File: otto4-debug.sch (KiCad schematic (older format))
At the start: 1 part

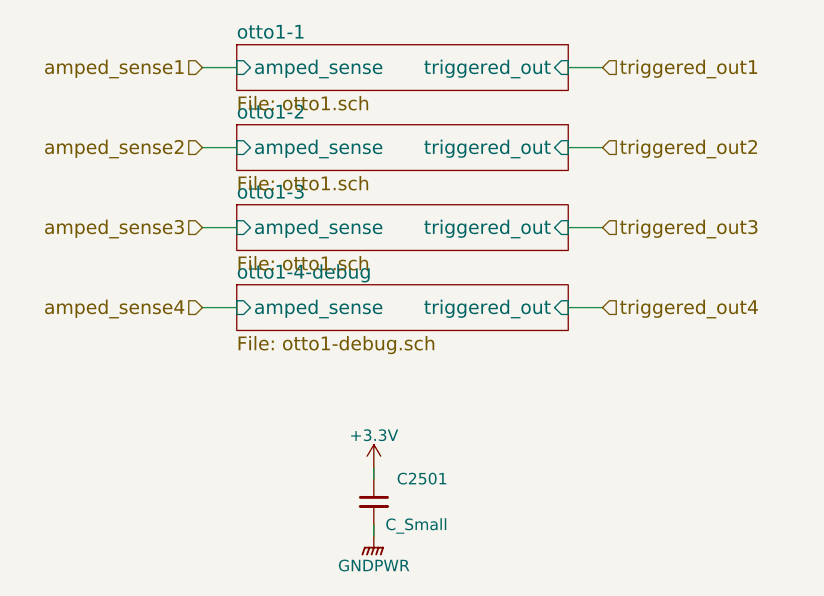
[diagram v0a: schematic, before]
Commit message: fixed debug pin going to multiple units
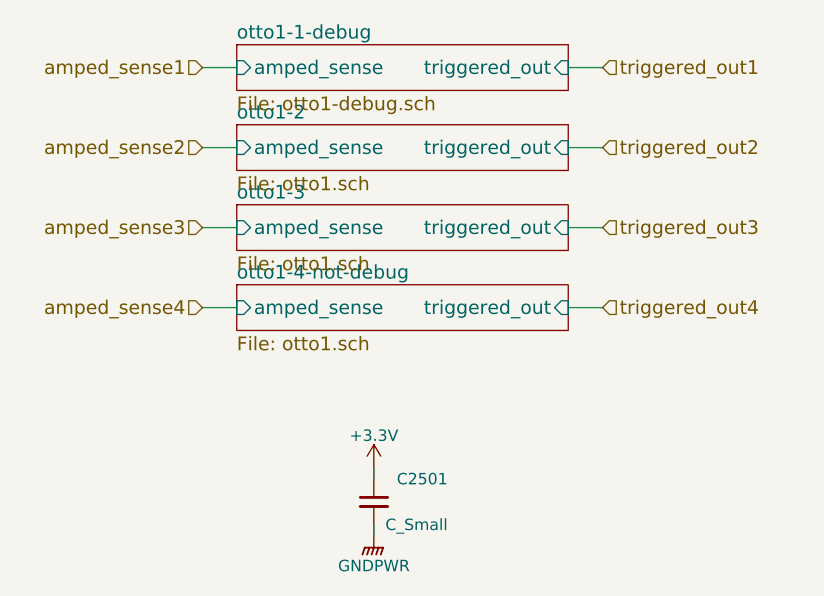
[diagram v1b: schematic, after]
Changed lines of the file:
@@
 $Sheet
 S 1550 1750 1450 200
-U 5AFCC6B4
-F0 "otto1-1" 60
-F1 "otto1.sch" 60
+U 5B02385F
+F0 "otto1-1-debug" 60
+F1 "otto1-debug.sch" 60
 F2 "amped_sense" I L 1550 1850 60
 F3 "triggered_out" I R 3000 1850 60
@@
 S 1550 2800 1450 200
 U 5AFCD579
-F0 "otto1-4-debug" 60
-F1 "otto1-debug.sch" 60
+F0 "otto1-4-not-debug" 60
+F1 "otto1.sch" 60
 F2 "amped_sense" I L 1550 2900 60
 F3 "triggered_out" I R 3000 2900 60
@@
 $Comp
 L C_Small C2501
-U 1 1 5B007FCB
+U 1 1 5B02386C
 P 2150 3750
-AR Path="/5AFCE970/5AFFB716/5AFCC2D5/5B007FCB" Ref="C2501"  Part="1"
-AR Path="/5AFCE970/5AFFB716/5AFCF0A3/5B007FCB" Ref="C3001"  Part="1"
-AR Path="/5AFCE970/5AFFB716/5AFD08C6/5B007FCB" Ref="C3501"  Part="1"
 F 0 "C2501" H 2250 3850 50  0000 L CNN
 F 1 "C_Small" H 2200 3650 50  0000 L CNN
@@
 $Comp
 L +3.3V #PWR?
-U 1 1 5B007FD7
+U 1 1 5B02386D
 P 2150 3600
-AR Path="/5AFCE970/5AFFB716/5AFCC2D5/5B007FD7" Ref="#PWR?"  Part="1"
-AR Path="/5AFCE970/5AFFB716/5AFCF0A3/5B007FD7" Ref="#PWR?"  Part="1"
-AR Path="/5AFCE970/5AFFB716/5AFD08C6/5B007FD7" Ref="#PWR?"  Part="1"
 F 0 "#PWR?" H 2150 3450 50  0001 C CNN
 F 1 "+3.3V" H 2150 3740 50  0000 C CNN
@@
 $Comp
 L GNDPWR #PWR?
-U 1 1 5B0088D8
+U 1 1 5B02386E
 P 2150 3900
-AR Path="/5AFCE970/5AFFB716/5AFCC2D5/5B0088D8" Ref="#PWR?"  Part="1"
-AR Path="/5AFCE970/5AFFB716/5AFCF0A3/5B0088D8" Ref="#PWR?"  Part="1"
-AR Path="/5AFCE970/5AFFB716/5AFD08C6/5B0088D8" Ref="#PWR?"  Part="1"
 F 0 "#PWR?" H 2150 3700 50  0001 C CNN
 F 1 "GNDPWR" H 2150 3770 50  0000 C CNN

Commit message: debugging is on lowest channel now
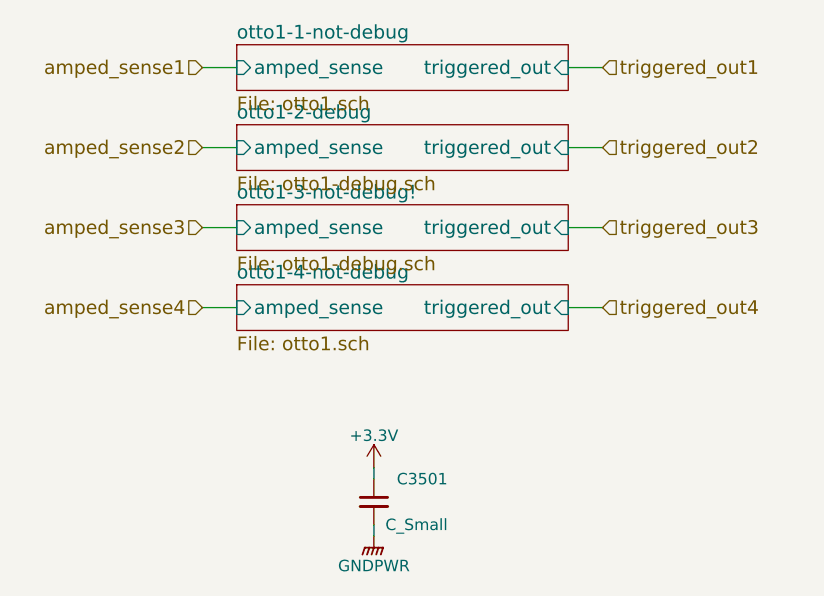
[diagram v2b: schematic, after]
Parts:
- renumbered C2501 to C3501
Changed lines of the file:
@@
 $Descr A4 11693 8268
 encoding utf-8
-Sheet 25 41
+Sheet 35 41
 Title ""
 Date ""
@@
 S 1550 1750 1450 200
 U 5B02385F
-F0 "otto1-1-debug" 60
-F1 "otto1-debug.sch" 60
+F0 "otto1-1-not-debug" 60
+F1 "otto1.sch" 60
 F2 "amped_sense" I L 1550 1850 60
 F3 "triggered_out" I R 3000 1850 60
@@
 S 1550 2100 1450 200
 U 5AFCD431
-F0 "otto1-2" 60
-F1 "otto1.sch" 60
+F0 "otto1-2-debug" 60
+F1 "otto1-debug.sch" 60
 F2 "amped_sense" I L 1550 2200 60
 F3 "triggered_out" I R 3000 2200 60
@@
 S 1550 2450 1450 200
 U 5AFCD50F
-F0 "otto1-3" 60
-F1 "otto1.sch" 60
+F0 "otto1-3-not-debug!" 60
+F1 "otto1-debug.sch" 60
 F2 "amped_sense" I L 1550 2550 60
 F3 "triggered_out" I R 3000 2550 60
@@
 	3000 2900 3150 2900
 $Comp
-L C_Small C2501
+L C_Small C3501
 U 1 1 5B02386C
 P 2150 3750
-F 0 "C2501" H 2250 3850 50  0000 L CNN
+F 0 "C3501" H 2250 3850 50  0000 L CNN
 F 1 "C_Small" H 2200 3650 50  0000 L CNN
 F 2 "Resistors_SMD:R_0805_HandSoldering" H 2150 3750 50  0001 C CNN

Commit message: started on routing triggers to blue pill
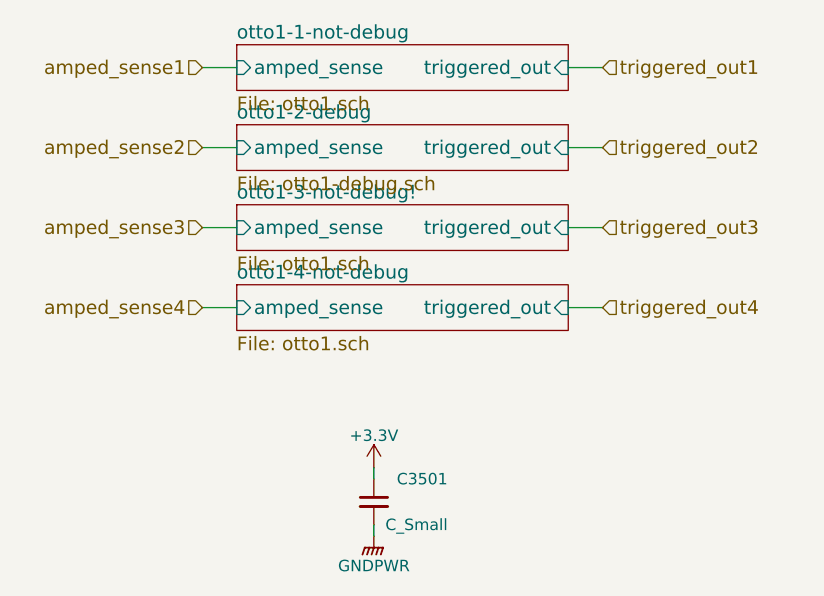
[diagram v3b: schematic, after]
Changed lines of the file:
@@
 U 5AFCD50F
 F0 "otto1-3-not-debug!" 60
-F1 "otto1-debug.sch" 60
+F1 "otto1.sch" 60
 F2 "amped_sense" I L 1550 2550 60
 F3 "triggered_out" I R 3000 2550 60

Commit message: set all passives values
I set them equal to or corresponding to the prototype performance.
to gain speed both signal caps should be decreased
to gain sensitivity the positive feedback resistor needs to be increased
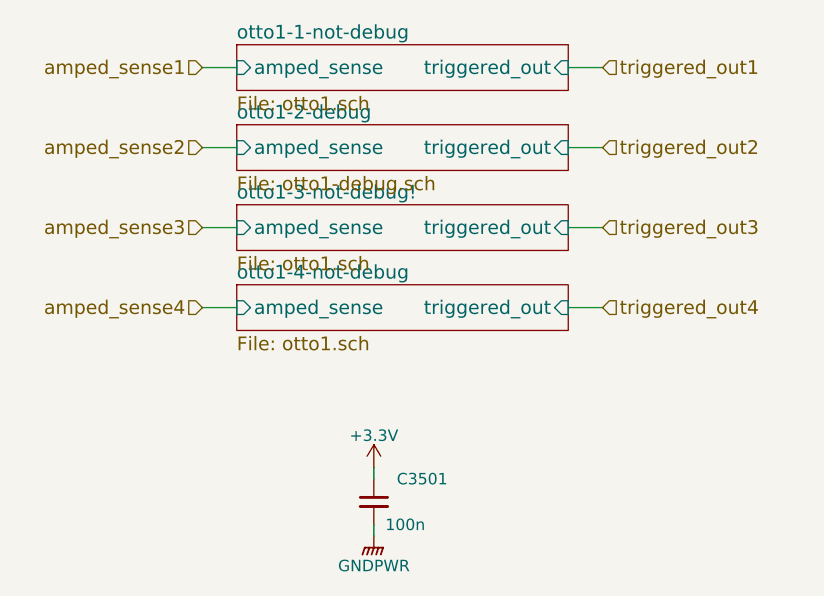
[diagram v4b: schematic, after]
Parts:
- C3501: value C_Small -> 100n
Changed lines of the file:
@@
 P 2150 3750
 F 0 "C3501" H 2250 3850 50  0000 L CNN
-F 1 "C_Small" H 2200 3650 50  0000 L CNN
+F 1 "100n" H 2200 3650 50  0000 L CNN
 F 2 "Resistors_SMD:R_0805_HandSoldering" H 2150 3750 50  0001 C CNN
 F 3 "" H 2150 3750 50  0001 C CNN
@@
 $EndComp
 $Comp
-L +3.3V #PWR?
+L +3.3V #PWR085
 U 1 1 5B02386D
 P 2150 3600
-F 0 "#PWR?" H 2150 3450 50  0001 C CNN
+F 0 "#PWR085" H 2150 3450 50  0001 C CNN
 F 1 "+3.3V" H 2150 3740 50  0000 C CNN
 F 2 "" H 2150 3600 50  0000 C CNN
@@
 $EndComp
 $Comp
-L GNDPWR #PWR?
+L GNDPWR #PWR086
 U 1 1 5B02386E
 P 2150 3900
-F 0 "#PWR?" H 2150 3700 50  0001 C CNN
+F 0 "#PWR086" H 2150 3700 50  0001 C CNN
 F 1 "GNDPWR" H 2150 3770 50  0000 C CNN
 F 2 "" H 2150 3850 50  0000 C CNN
